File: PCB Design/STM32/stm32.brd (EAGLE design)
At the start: 71.1 x 84.3 mm, 68 parts, among them IC1 NCP1117ST50T3G, Q1 ABM3B-8.000MHZ-10-1UT, T1 SFH303, T2 SFH303, T3 SFH303, T4 SFH303, T5 BC847, T6 BC847, T7 BC847, T8 BC847, U1 STM32F103RET6, U2 MCP1700T-3302E/TT, U3 MCP1700T-3302E/TT, U4 MPU-6050, U5 TB6612FNG, X1 22-23-2031

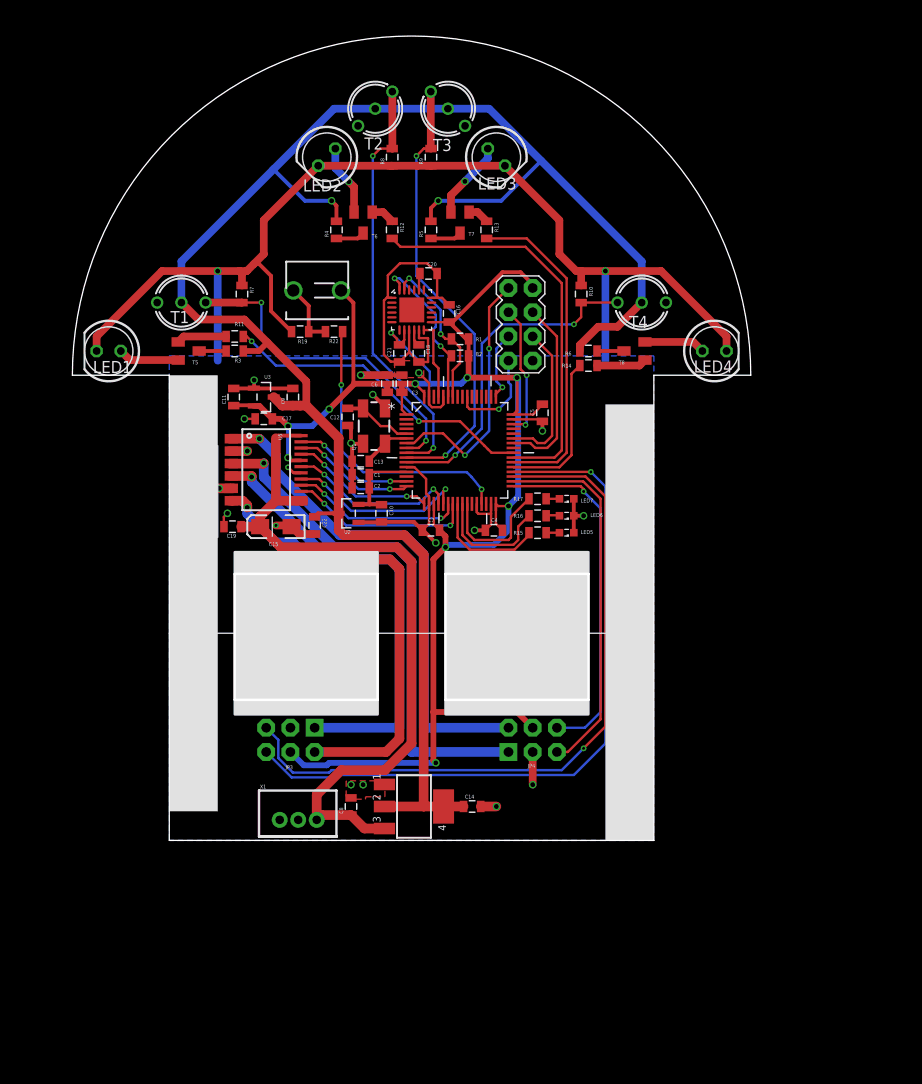
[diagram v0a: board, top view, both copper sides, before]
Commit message: changed to new phototransistors
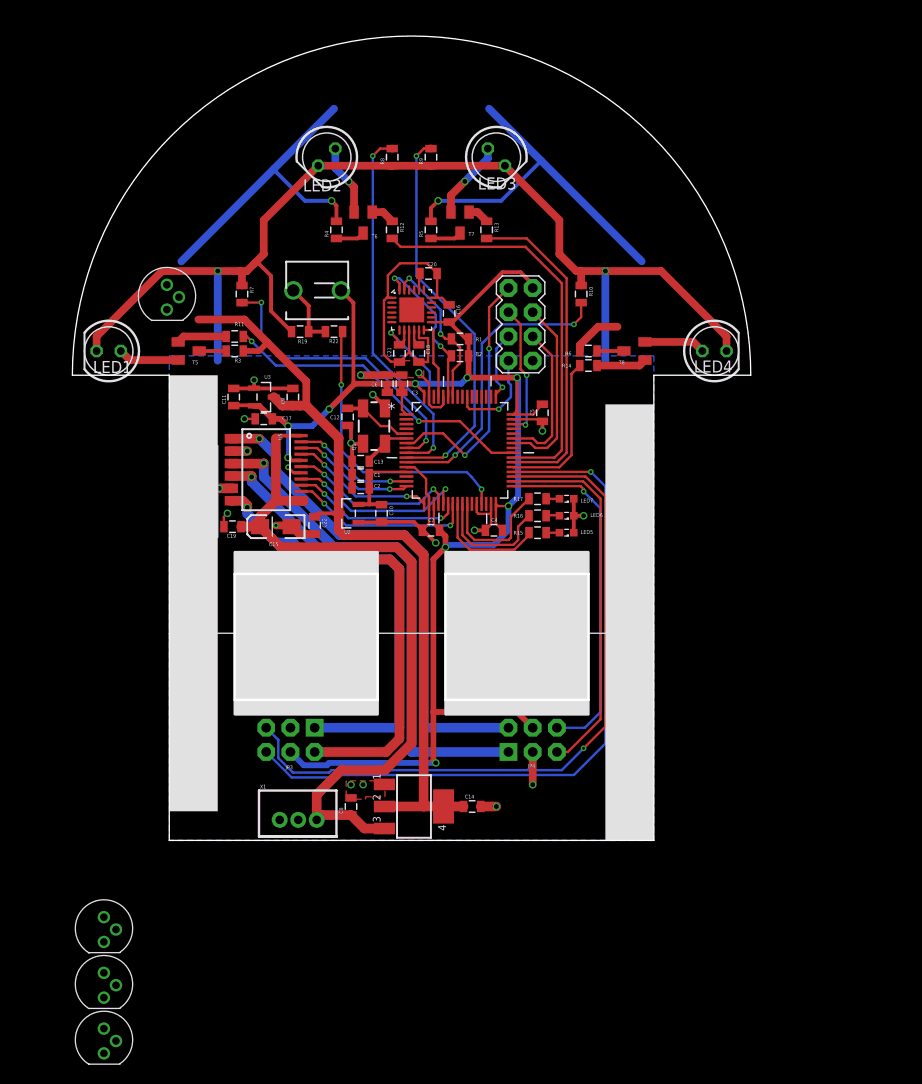
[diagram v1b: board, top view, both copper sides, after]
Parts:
- removed T1, T2, T3, T4: SFH303, opto-trans-siemens:SFH303
- added U$2, U$3, U$4, U$5: PHTRST, phototransistor:PHTRST
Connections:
- net 5V: now also U$2.P$C, U$3.P$C, U$4.P$C, U$5.P$C; no longer T1.2, T2.2, T3.2, T4.2
- net IR_IN1: now also U$2.P$E; no longer T1.1
- net IR_IN2: now also U$3.P$E; no longer T2.1
- net IR_IN3: now also U$4.P$E; no longer T3.1
- net IR_IN4: now also U$5.P$E; no longer T4.1
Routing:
- net 5V: track 192.7 -> 161.7 mm
- net IR_IN2: track 44.6 -> 38.6 mm
- net IR_IN3: track 47.2 -> 41.2 mm
- net IR_IN4: track 35.2 -> 31.3 mm
- net IR_IN1: track 35.1 -> 31.3 mm
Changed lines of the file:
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@@
 <element name="R8" library="SparkFun-Resistors" package="0805" value="42 Ohm" x="35.814" y="74.422" rot="R90"/>
 <element name="R9" library="SparkFun-Resistors" package="0805" value="42 Ohm" x="39.878" y="74.422" rot="R90"/>
-<element name="T1" library="opto-trans-siemens" package="SFH303" value="SFH303" x="13.716" y="59.182" smashed="yes" rot="R270">
-<attribute name="OC_NEWARK" value="unknown" x="13.716" y="59.182" size="1.778" layer="27" rot="R270" display="off"/>
-<attribute name="MPN" value="" x="13.716" y="59.182" size="1.778" layer="27" rot="R270" display="off"/>
-<attribute name="MF" value="" x="13.716" y="59.182" size="1.778" layer="27" rot="R270" display="off"/>
-<attribute name="OC_FARNELL" value="unknown" x="13.716" y="59.182" size="1.778" layer="27" rot="R270" display="off"/>
-<attribute name="NAME" x="12.573" y="57.023" size="1.27" layer="25"/>
-</element>
-<element name="T2" library="opto-trans-siemens" package="SFH303" value="SFH303" x="34.036" y="79.502" smashed="yes" rot="R315">
-<attribute name="OC_NEWARK" value="unknown" x="34.036" y="79.502" size="1.778" layer="27" rot="R315" display="off"/>
-<attribute name="MPN" value="" x="34.036" y="79.502" size="1.778" layer="27" rot="R315" display="off"/>
-<attribute name="MF" value="" x="34.036" y="79.502" size="1.778" layer="27" rot="R315" display="off"/>
-<attribute name="OC_FARNELL" value="unknown" x="34.036" y="79.502" size="1.778" layer="27" rot="R315" display="off"/>
-<attribute name="NAME" x="32.902028125" y="75.220103125" size="1.27" layer="25"/>
-</element>
-<element name="T3" library="opto-trans-siemens" package="SFH303" value="SFH303" x="41.656" y="79.502" smashed="yes" rot="R45">
-<attribute name="OC_NEWARK" value="unknown" x="41.656" y="79.502" size="1.778" layer="27" rot="R45" display="off"/>
-<attribute name="MPN" value="" x="41.656" y="79.502" size="1.778" layer="27" rot="R45" display="off"/>
-<attribute name="MF" value="" x="41.656" y="79.502" size="1.778" layer="27" rot="R45" display="off"/>
-<attribute name="OC_FARNELL" value="unknown" x="41.656" y="79.502" size="1.778" layer="27" rot="R45" display="off"/>
-<attribute name="NAME" x="40.095896875" y="75.066025" size="1.27" layer="25"/>
-</element>
-<element name="T4" library="opto-trans-siemens" package="SFH303" value="SFH303" x="61.976" y="59.182" smashed="yes" rot="R90">
-<attribute name="OC_NEWARK" value="unknown" x="61.976" y="59.182" size="1.778" layer="27" rot="R90" display="off"/>
-<attribute name="MPN" value="" x="61.976" y="59.182" size="1.778" layer="27" rot="R90" display="off"/>
-<attribute name="MF" value="" x="61.976" y="59.182" size="1.778" layer="27" rot="R90" display="off"/>
-<attribute name="OC_FARNELL" value="unknown" x="61.976" y="59.182" size="1.778" layer="27" rot="R90" display="off"/>
-<attribute name="NAME" x="62.611" y="57.785" size="1.27" layer="25" rot="R180"/>
-</element>
 <element name="U1" library="ST Microelctronics_By_element14_Batch_1" package="QFP50P1200X1200X160-64N" value="STM32F103RET6" x="42.926" y="43.688" smashed="yes">
 <attribute name="PACKAGE" value="QFP-64" x="42.926" y="43.688" size="1.778" layer="27" display="off"/>
@@
 <attribute name="VALUE" x="64.389" y="52.197" size="1.27" layer="27" rot="R90"/>
 </element>
+<element name="U$2" library="phototransistor" package="PHTRST" value="PHTRST" x="12.192" y="59.944"/>
+<element name="U$3" library="phototransistor" package="PHTRST" value="PHTRST" x="5.588" y="-6.35"/>
+<element name="U$4" library="phototransistor" package="PHTRST" value="PHTRST" x="5.588" y="-12.192"/>
+<element name="U$5" library="phototransistor" package="PHTRST" value="PHTRST" x="5.588" y="-18.034"/>
 </elements>
 <signals>
@@
 <signal name="IR_IN1">
 <contactref element="U1" pad="8"/>
-<contactref element="T1" pad="1"/>
 <contactref element="R7" pad="2"/>
-<wire x1="16.256" y1="59.182" x2="20.055" y2="59.182" width="0.8128" layer="1"/>
 <wire x1="20.055" y1="59.182" x2="20.066" y2="59.171" width="0.8128" layer="1"/>
 <wire x1="37.3126" y1="43.942" x2="38.608" y2="43.942" width="0.254" layer="1"/>
@@
 <wire x1="24.13" y1="53.34" x2="22.098" y2="55.372" width="0.254" layer="16"/>
 <wire x1="22.098" y1="55.372" x2="22.098" y2="59.182" width="0.254" layer="16"/>
+<contactref element="U$2" pad="P$E"/>
+<wire x1="12.192" y1="58.444" x2="37.3126" y2="43.942" width="0" layer="19" extent="1-1"/>
 </signal>
 <signal name="IR_IN2">
 <contactref element="U1" pad="9"/>
-<contactref element="T2" pad="1"/>
 <contactref element="R8" pad="2"/>
 <wire x1="37.3126" y1="43.434" x2="39.624" y2="43.434" width="0.254" layer="1"/>
@@
 <wire x1="33.782" y1="53.848" x2="33.782" y2="74.549" width="0.254" layer="16"/>
 <via x="33.782" y="74.549" extent="1-16" drill="0.3048"/>
-<wire x1="35.83205" y1="81.29805" x2="35.83205" y2="75.322" width="0.8128" layer="1"/>
 <wire x1="35.83205" y1="75.322" x2="35.814" y2="75.322" width="0.8128" layer="1"/>
 <wire x1="33.782" y1="74.549" x2="34.544" y2="75.322" width="0.254" layer="1"/>
 <wire x1="34.544" y1="75.322" x2="35.814" y2="75.322" width="0.254" layer="1"/>
+<contactref element="U$3" pad="P$E"/>
+<wire x1="5.588" y1="-7.85" x2="37.3126" y2="43.434" width="0" layer="19" extent="1-1"/>
 </signal>
 <signal name="IR_IN3">
 <contactref element="U1" pad="10"/>
-<contactref element="T3" pad="1"/>
 <contactref element="R9" pad="2"/>
 <via x="41.402" y="43.18" extent="1-16" drill="0.3048"/>
@@
 <wire x1="37.3126" y1="42.926" x2="41.148" y2="42.926" width="0.254" layer="1"/>
 <wire x1="41.148" y1="42.926" x2="41.402" y2="43.18" width="0.254" layer="1"/>
-<wire x1="39.859946875" y1="81.29805" x2="39.859946875" y2="75.340053125" width="0.8128" layer="1"/>
 <wire x1="39.859946875" y1="75.340053125" x2="39.878" y2="75.322" width="0.8128" layer="1"/>
 <wire x1="38.354" y1="74.549" x2="39.127" y2="75.322" width="0.254" layer="1"/>
 <wire x1="39.127" y1="75.322" x2="39.878" y2="75.322" width="0.254" layer="1"/>
+<contactref element="U$4" pad="P$E"/>
+<wire x1="5.588" y1="-13.692" x2="37.3126" y2="42.926" width="0" layer="19" extent="1-1"/>
 </signal>
 <signal name="IR_IN4">
 <contactref element="U1" pad="11"/>
-<contactref element="T4" pad="1"/>
 <contactref element="R10" pad="2"/>
-<wire x1="59.436" y1="59.182" x2="55.626" y2="59.182" width="0.254" layer="1"/>
 <wire x1="55.626" y1="59.182" x2="55.626" y2="59.171" width="0.254" layer="1"/>
 <via x="42.418" y="43.18" extent="1-16" drill="0.3048"/>
@@
 <wire x1="42.418" y1="43.18" x2="41.6814" y2="42.4434" width="0.254" layer="1"/>
 <wire x1="41.6814" y1="42.4434" x2="37.3126" y2="42.4434" width="0.254" layer="1"/>
+<contactref element="U$5" pad="P$E"/>
+<wire x1="5.588" y1="-19.534" x2="37.3126" y2="42.4434" width="0" layer="19" extent="1-1"/>
 </signal>
 <signal name="IR_OUT2">
@@
 <signal name="5V">
 <contactref element="U3" pad="3"/>
-<contactref element="T1" pad="2"/>
-<contactref element="T2" pad="2"/>
-<contactref element="T3" pad="2"/>
-<contactref element="T4" pad="2"/>
 <contactref element="IC1" pad="2"/>
 <contactref element="IC1" pad="4"/>
@@
 <wire x1="30.2006" y1="35.3314" x2="30.734" y2="34.798" width="1.016" layer="1"/>
 <wire x1="30.734" y1="34.798" x2="37.084" y2="34.798" width="1.016" layer="1"/>
-<wire x1="13.716" y1="59.182" x2="13.716" y2="63.5" width="0.8128" layer="16"/>
 <wire x1="13.716" y1="63.5" x2="23.368" y2="73.152" width="0.8128" layer="16"/>
 <wire x1="23.368" y1="73.152" x2="29.718" y2="79.502" width="0.8128" layer="16"/>
-<wire x1="29.718" y1="79.502" x2="34.036" y2="79.502" width="0.8128" layer="16"/>
-<wire x1="34.036" y1="79.502" x2="41.656" y2="79.502" width="0.8128" layer="16"/>
-<wire x1="61.976" y1="59.182" x2="61.976" y2="63.5" width="0.8128" layer="16"/>
 <wire x1="61.976" y1="63.5" x2="51.435" y2="74.041" width="0.8128" layer="16"/>
 <wire x1="51.435" y1="74.041" x2="45.974" y2="79.502" width="0.8128" layer="16"/>
-<wire x1="45.974" y1="79.502" x2="41.656" y2="79.502" width="0.8128" layer="16"/>
 <wire x1="30.2006" y1="37.084" x2="28.056" y2="37.084" width="0.4064" layer="1"/>
 <wire x1="28.056" y1="37.084" x2="27.686" y2="36.714" width="0.4064" layer="1"/>
@@
 <wire x1="29.972" y1="67.702" x2="29.972" y2="69.342" width="0.4064" layer="1"/>
 <wire x1="29.972" y1="69.342" x2="29.464" y2="69.85" width="0.4064" layer="1"/>
-<wire x1="13.716" y1="59.182" x2="15.494" y2="57.404" width="0.8128" layer="1"/>
 <wire x1="15.494" y1="57.404" x2="20.32" y2="57.404" width="0.8128" layer="1"/>
 <wire x1="26.808" y1="50.916" x2="26.808" y2="48.376" width="0.8128" layer="1"/>
 <wire x1="35.0012" y1="6.35" x2="39.116" y2="6.35" width="1.016" layer="1"/>
 <wire x1="39.116" y1="6.35" x2="41.199" y2="6.35" width="1.016" layer="1"/>
-<wire x1="61.976" y1="59.182" x2="59.436" y2="56.642" width="0.8128" layer="1"/>
 <wire x1="59.436" y1="56.642" x2="57.404" y2="56.642" width="0.8128" layer="1"/>
 <wire x1="57.404" y1="56.642" x2="55.488" y2="54.726" width="0.8128" layer="1"/>
@@
 <wire x1="20.204" y1="54.102" x2="21.844" y2="54.102" width="0.6096" layer="1"/>
 <wire x1="21.844" y1="54.102" x2="22.733" y2="54.991" width="0.6096" layer="1"/>
+<contactref element="U$2" pad="P$C"/>
+<contactref element="U$3" pad="P$C"/>
+<contactref element="U$4" pad="P$C"/>
+<contactref element="U$5" pad="P$C"/>
+<wire x1="61.976" y1="63.5" x2="59.436" y2="56.642" width="0" layer="19" extent="1-16"/>
+<wire x1="29.972" y1="67.702" x2="39.878" y2="67.702" width="0" layer="19" extent="1-1"/>
+<wire x1="15.494" y1="57.404" x2="13.716" y2="63.5" width="0" layer="19" extent="1-16"/>
+<wire x1="13.462" y1="59.744" x2="35.0012" y2="6.35" width="0" layer="19" extent="1-1"/>
+<wire x1="6.858" y1="-6.55" x2="13.462" y2="59.744" width="0" layer="19" extent="1-1"/>
+<wire x1="6.858" y1="-12.392" x2="6.858" y2="-6.55" width="0" layer="19" extent="1-1"/>
+<wire x1="6.858" y1="-18.234" x2="6.858" y2="-12.392" width="0" layer="19" extent="1-1"/>
 </signal>
 <signal name="N$1">
